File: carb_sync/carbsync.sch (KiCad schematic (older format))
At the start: 49 parts, among them IC1 ATMEGA328P-A, P1 CONN_02X03, P2 CONN_01X02, SW1 SPST, SW2 SPST, SW3 SPST, SW4 SPST, U1 MPXV6115V, U2 MPXV6115V, U3 MPXV6115V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

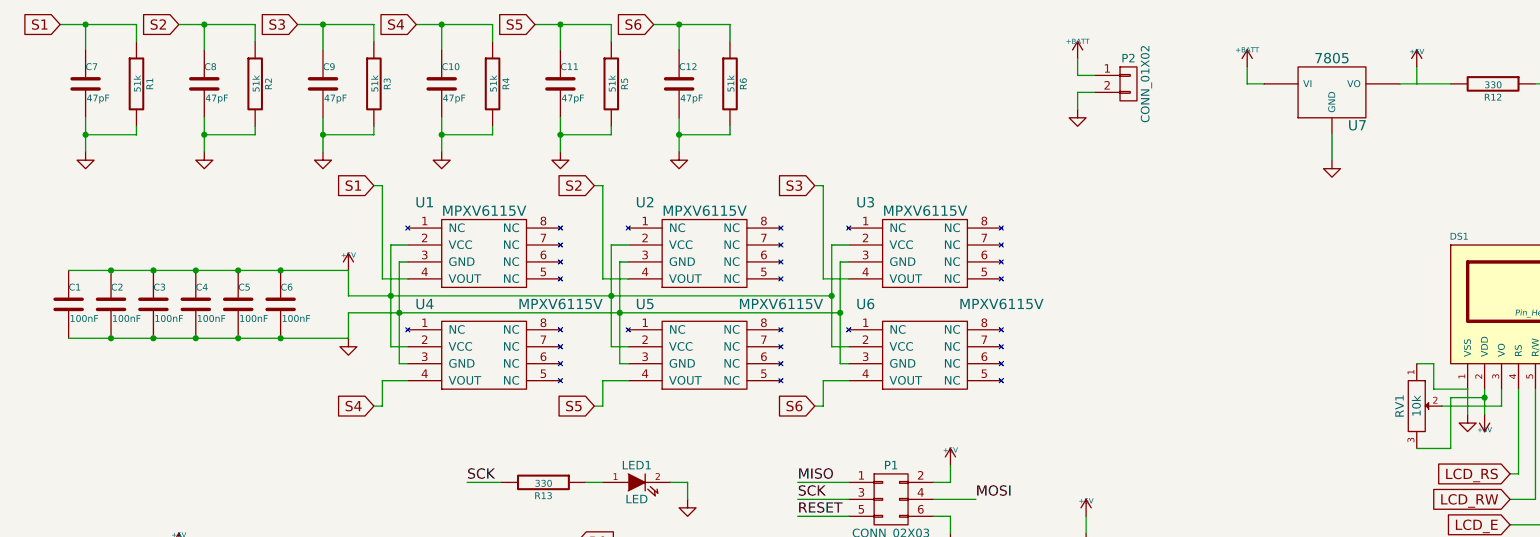
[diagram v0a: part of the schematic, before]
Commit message: [carb_sync] Initial complete layout. LCD connector to pads.
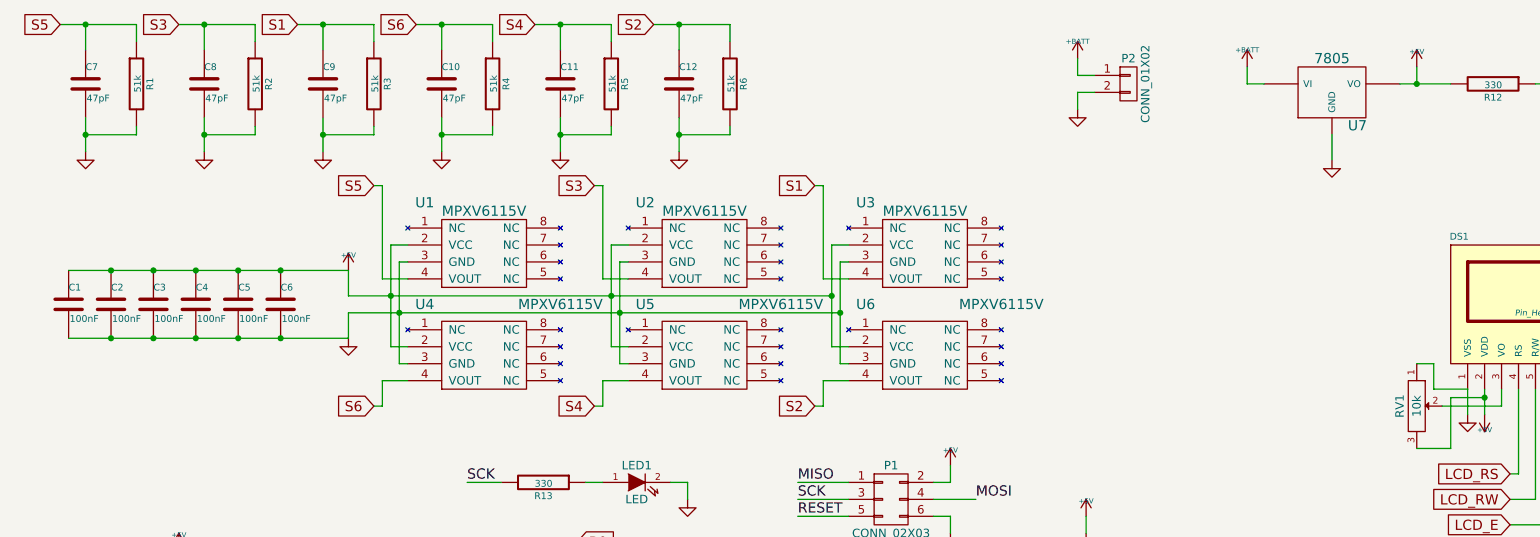
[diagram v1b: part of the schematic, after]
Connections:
- net +5V: now also R12.2, U7.VO
- net S1: now also C9.1, R3.1, U3.4 (VOUT); no longer C7.1, R1.1, U1.4 (VOUT)
- net S2: now also C12.1, R6.1, U6.4 (VOUT); no longer C8.1, R2.1, U2.4 (VOUT)
- net S3: now also C8.1, R2.1, U2.4 (VOUT); no longer C9.1, R3.1, U3.4 (VOUT)
- net S4: now also C11.1, R5.1, U5.4 (VOUT); no longer C10.1, R4.1, U4.4 (VOUT)
- net S5: now also C7.1, R1.1, U1.4 (VOUT); no longer C11.1, R5.1, U5.4 (VOUT)
- net S6: now also C10.1, R4.1, U4.4 (VOUT); no longer C12.1, R6.1, U6.4 (VOUT)
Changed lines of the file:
@@
 $EndComp
 Text GLabel 2650 1550 0    60   Input ~ 0
+S5
+Text GLabel 3950 1550 0    60   Input ~ 0
+S3
+Text GLabel 5250 1550 0    60   Input ~ 0
 S1
-Text GLabel 3950 1550 0    60   Input ~ 0
+Text GLabel 2650 2850 0    60   Input ~ 0
+S6
+Text GLabel 3950 2850 0    60   Input ~ 0
+S4
+Text GLabel 5250 2850 0    60   Input ~ 0
 S2
-Text GLabel 5250 1550 0    60   Input ~ 0
-S3
-Text GLabel 2650 2850 0    60   Input ~ 0
-S4
-Text GLabel 3950 2850 0    60   Input ~ 0
+Text GLabel 800  600  0    60   Input ~ 0
 S5
-Text GLabel 5250 2850 0    60   Input ~ 0
-S6
-Text GLabel 800  600  0    60   Input ~ 0
-S1
 $Comp
 L C C7
@@
 $EndComp
 Text GLabel 1500 600  0    60   Input ~ 0
-S2
+S3
 $Comp
 L C C8
@@
 $EndComp
 Text GLabel 2200 600  0    60   Input ~ 0
-S3
+S1
 $Comp
 L C C9
@@
 $EndComp
 Text GLabel 2900 600  0    60   Input ~ 0
-S4
+S6
 $Comp
 L C C10
@@
 $EndComp
 Text GLabel 3600 600  0    60   Input ~ 0
-S5
+S4
 $Comp
 L C C11
@@
 $EndComp
 Text GLabel 4300 600  0    60   Input ~ 0
-S6
+S2
 $Comp
 L C C12
@@
 $EndComp
 $Comp
-L +5V #5V010
+L +5V #010
 U 1 1 54D72143
 P 8800 850
-F 0 "#5V010" H 8800 940 20  0001 C CNN
+F 0 "#010" H 8800 940 20  0001 C CNN
 F 1 "+5V" H 8800 940 30  0000 C CNN
 F 2 "" H 8800 850 60  0000 C CNN
@@
 Wire Wire Line
 	8700 950  9000 950
-Wire Wire Line
-	8800 950  8800 850
 Wire Wire Line
 	7800 850  7800 950
@@
 Wire Wire Line
 	6800 1000 6800 1100
+Wire Wire Line
+	8800 850  8800 950
+Connection ~ 8800 950
 $EndSCHEMATC

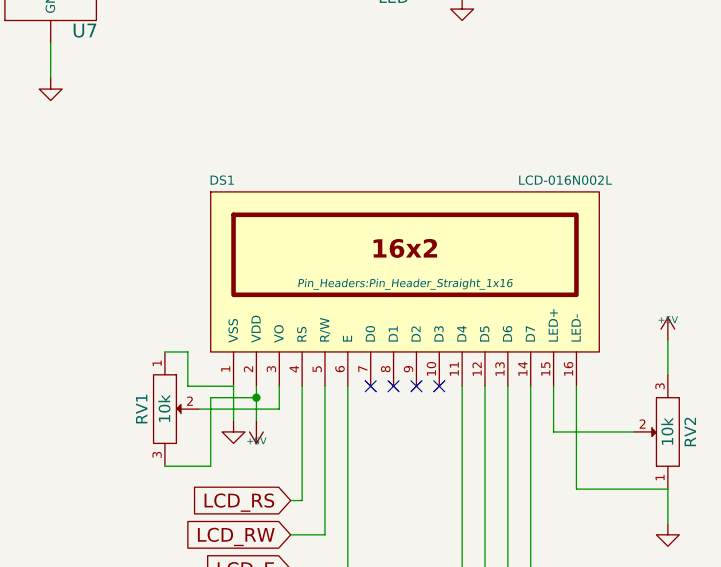
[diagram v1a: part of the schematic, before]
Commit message: [carb_sync] Changed crystal footprint for ATMEGA328P.
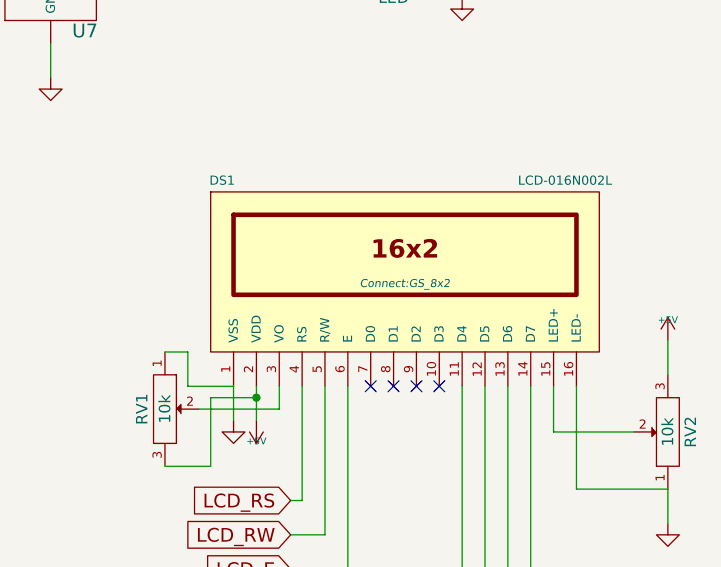
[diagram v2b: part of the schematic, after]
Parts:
- DS1: footprint Pin_Headers:Pin_Header_Straight_1x16 -> Connect:GS_8x2
- X1: footprint Crystals:Crystal_HC52-U_Vertical -> NQBit:HC-49USX_SMD
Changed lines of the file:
@@
 F 0 "X1" H 4500 4650 60  0000 C CNN
 F 1 "CRYSTAL" H 4500 4350 60  0000 C CNN
-F 2 "Crystals:Crystal_HC52-U_Vertical" H 4500 4500 60  0001 C CNN
+F 2 "NQBit:HC-49USX_SMD" H 4500 4500 60  0001 C CNN
 F 3 "" H 4500 4500 60  0000 C CNN
 	1    4500 4500
@@
 F 0 "DS1" H 9050 2650 40  0000 C CNN
 F 1 "LCD-016N002L" H 10550 2650 40  0000 C CNN
-F 2 "Pin_Headers:Pin_Header_Straight_1x16" H 9850 2200 35  0000 C CIN
+F 2 "Connect:GS_8x2" H 9850 2200 35  0000 C CIN
 F 3 "" H 9850 2250 60  0000 C CNN
 	1    9850 2250
